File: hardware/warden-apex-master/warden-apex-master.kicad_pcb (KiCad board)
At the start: 4 copper layers, 100 x 100 mm, 88 parts, among them IC1 SIM7080G, IC2 BQ24650RVAR, IC3 TPS63070RNMR, IC4 MAX98357AETE+T, J1 U.FL-R-SMT-1, J2 U.FL-R-SMT-1, J3 61300211121, J4 Expansion_Header, J5 Qwiic, Q1 DMG9926UDM, Q2 AO3401A, Q3 2N7002, U1 113991115, U2 Ai-Thinker-Ra-01, U3 M138 Modem, U4 MCP23017_SO, U5 SRV05-4-P-T7, U6 SC16IS740, X1 14.7456MHz

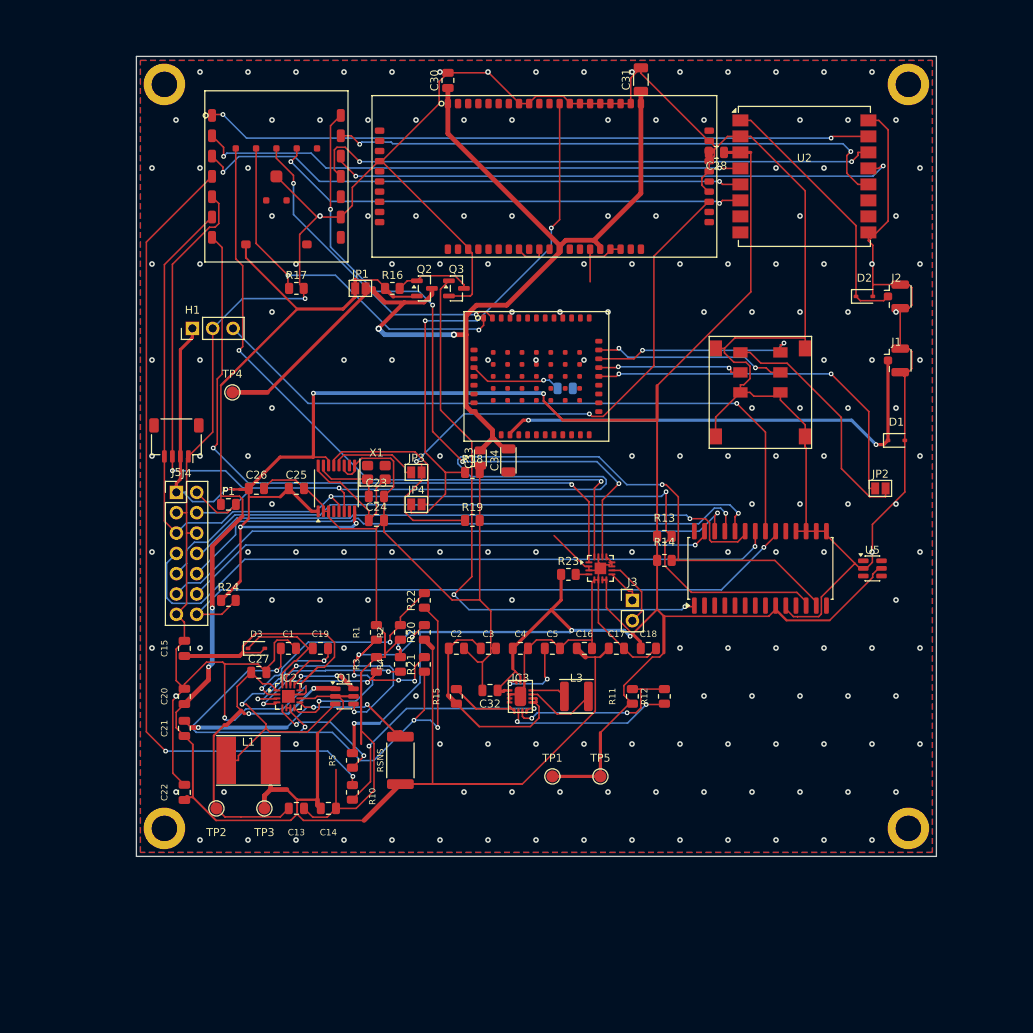
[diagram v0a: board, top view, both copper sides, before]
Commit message: Update warden-apex design to Phase 24 live state. Enhanced README.md to clarify current design status, noting that the snapshot is not yet production-ready. Adjusted BOM files to include additional resistors and capacitors, and updated component placements. Revised Gerber files with new timestamps and ensured consistency across documentation. Addressed DRC issues with 10 violations and 5 unconnected items, indicating further cleanup is required before production submission.
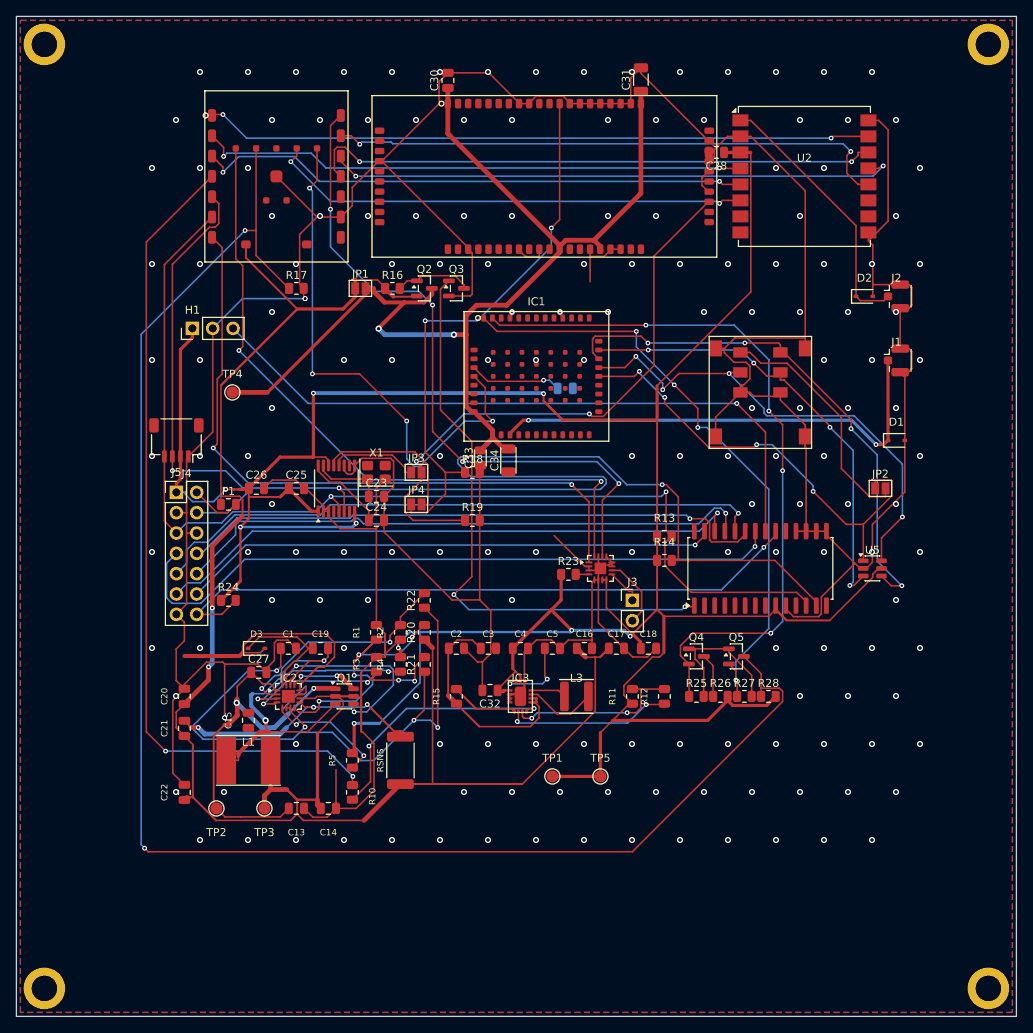
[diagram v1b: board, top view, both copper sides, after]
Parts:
- added Q4: SOT-23, SOT-23, F.Cu at (70.0, 75.0)
- added Q5: SOT-23, SOT-23, F.Cu at (75.0, 75.0)
- added R25: R_0805_2012Metric, R_0805_2012Metric, F.Cu at (70.0, 80.0)
- added R26: R_0805_2012Metric, R_0805_2012Metric, F.Cu at (73.0, 80.0)
- added R27: R_0805_2012Metric, R_0805_2012Metric, F.Cu at (76.0, 80.0)
- added R28: R_0805_2012Metric, R_0805_2012Metric, F.Cu at (79.0, 80.0)
- C31, C34: value 47uF -> 220uF
- IC1: value SIM7080G -> LCC-42_SIM7080G; footprint warden_custom:LCC-42_SIM7080G -> LCC-42_SIM7080G
- moved MH3 25.0 mm to (-11.5, 116.5)
- moved MH4 22.4 mm to (106.5, 116.5)
- moved MH1 15.8 mm to (-11.5, -1.50)
- moved C15 12.0 mm to (14.0, 83.0)
- moved MH2 11.2 mm to (106.5, -1.50)
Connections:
- IC1 pad 1: /UART1_RX -> /UART1_RX_1V8
- IC1 pad 2: /UART1_TX -> /UART1_TX_1V8
- J5 pad MP: (no net) -> /DUMMY_NET_PRESERVE_2
- MH1 pad : (no net) -> /DUMMY_NET_PRESERVE_0
- MH2 pad : (no net) -> /DUMMY_NET_PRESERVE_113
- MH3 pad : (no net) -> /DUMMY_NET_PRESERVE_114
- MH4 pad : (no net) -> /DUMMY_NET_PRESERVE_3
- U1 pad 12: (no net) -> /DUMMY_NET_PRESERVE_8
- U1 pad 14: (no net) -> /DUMMY_NET_PRESERVE_9
- U1 pad 16: (no net) -> /DUMMY_NET_PRESERVE_10
- U1 pad 21: (no net) -> /MODEM_PWRKEY_N
- U1 pad 22: (no net) -> /DUMMY_NET_PRESERVE_11
- U1 pad 23: (no net) -> /DUMMY_NET_PRESERVE_12
- U2 pad 10: (no net) -> /DUMMY_NET_PRESERVE_52
- U2 pad 11: (no net) -> /DUMMY_NET_PRESERVE_53
- U2 pad 7: (no net) -> /DUMMY_NET_PRESERVE_50
- U2 pad 8: (no net) -> /DUMMY_NET_PRESERVE_51
- U3 pad 10: (no net) -> /DUMMY_NET_PRESERVE_19
- U3 pad 11: (no net) -> /DUMMY_NET_PRESERVE_20
- U3 pad 2: (no net) -> /DUMMY_NET_PRESERVE_13
- U3 pad 21: (no net) -> /DUMMY_NET_PRESERVE_21
- U3 pad 26: (no net) -> /DUMMY_NET_PRESERVE_22
- U3 pad 29: (no net) -> /DUMMY_NET_PRESERVE_23
- U3 pad 3: (no net) -> /DUMMY_NET_PRESERVE_14
- U3 pad 30: (no net) -> /DUMMY_NET_PRESERVE_24
- U3 pad 31: (no net) -> /DUMMY_NET_PRESERVE_25
- U3 pad 32: (no net) -> /DUMMY_NET_PRESERVE_26
- U3 pad 37: (no net) -> /DUMMY_NET_PRESERVE_27
- U3 pad 38: (no net) -> /DUMMY_NET_PRESERVE_28
- U3 pad 4: (no net) -> /DUMMY_NET_PRESERVE_15
- U3 pad 40: (no net) -> /DUMMY_NET_PRESERVE_29
- U3 pad 42: (no net) -> /DUMMY_NET_PRESERVE_30
- U3 pad 44: (no net) -> /DUMMY_NET_PRESERVE_31
- U3 pad 45: (no net) -> /DUMMY_NET_PRESERVE_32
- U3 pad 46: (no net) -> /DUMMY_NET_PRESERVE_33
- U3 pad 47: (no net) -> /DUMMY_NET_PRESERVE_34
- U3 pad 49: (no net) -> /DUMMY_NET_PRESERVE_35
- U3 pad 5: (no net) -> /DUMMY_NET_PRESERVE_16
- U3 pad 50: (no net) -> /DUMMY_NET_PRESERVE_36
- U3 pad 51: (no net) -> /DUMMY_NET_PRESERVE_37
- U3 pad 52: (no net) -> /DUMMY_NET_PRESERVE_38
- U3 pad 53: (no net) -> /DUMMY_NET_PRESERVE_39
- U3 pad 54: (no net) -> /DUMMY_NET_PRESERVE_40
- U3 pad 55: (no net) -> /DUMMY_NET_PRESERVE_41
- U3 pad 56: (no net) -> /DUMMY_NET_PRESERVE_42
- U3 pad 58: (no net) -> /DUMMY_NET_PRESERVE_43
- U3 pad 59: (no net) -> /DUMMY_NET_PRESERVE_44
- U3 pad 6: (no net) -> /DUMMY_NET_PRESERVE_17
- U3 pad 60: (no net) -> /DUMMY_NET_PRESERVE_45
- U3 pad 7: (no net) -> /DUMMY_NET_PRESERVE_18
- U4 pad 11: (no net) -> /DUMMY_NET_PRESERVE_61
- U4 pad 14: (no net) -> /DUMMY_NET_PRESERVE_62
- U4 pad 19: (no net) -> /DUMMY_NET_PRESERVE_63
- U4 pad 2: (no net) -> /DUMMY_NET_PRESERVE_54
- U4 pad 28: (no net) -> /DUMMY_NET_PRESERVE_64
- U4 pad 3: (no net) -> /DUMMY_NET_PRESERVE_55
- U4 pad 4: (no net) -> /DUMMY_NET_PRESERVE_56
- U4 pad 5: (no net) -> /DUMMY_NET_PRESERVE_57
- U4 pad 6: (no net) -> /DUMMY_NET_PRESERVE_58
- U4 pad 7: (no net) -> /DUMMY_NET_PRESERVE_59
- U4 pad 8: (no net) -> /DUMMY_NET_PRESERVE_60
- U5 pad 1: (no net) -> /SIM_VDD
- U5 pad 3: (no net) -> /SIM_DATA
- U5 pad 4: (no net) -> /SIM_CLK
- U5 pad 6: (no net) -> /SIM_RST
- U6 pad 10: (no net) -> /DUMMY_NET_PRESERVE_67
- U6 pad 4: (no net) -> /DUMMY_NET_PRESERVE_65
- U6 pad 7: (no net) -> /DUMMY_NET_PRESERVE_66
- X1 pad 3: (no net) -> /DUMMY_NET_PRESERVE_111
- X1 pad 4: (no net) -> /DUMMY_NET_PRESERVE_112
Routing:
- net /UART1_RX: track 47.7 -> 201.1 mm
- net /UART1_TX_1V8: track 0.00 -> 91.0 mm, vias 0 -> 4
- net /UART1_RX_1V8: track 0.00 -> 77.1 mm, vias 0 -> 4
- net /MODEM_PWRKEY_N: track 0.00 -> 67.7 mm, vias 0 -> 4
- net /SIM_RST: track 18.2 -> 61.2 mm, vias 2 -> 4
- net /SIM_CLK: track 25.5 -> 66.8 mm, vias 2 -> 4
- net /UART1_TX: track 39.7 -> 5.48 mm, vias 2 -> 0
- net /SIM_DATA: track 24.0 -> 57.1 mm, vias 2 -> 4
- net /3V3: track 404.5 -> 427.1 mm
- net /VDD_EXT: track 0.00 -> 18.5 mm
- net /SIM_VDD: track 46.2 -> 57.2 mm, vias 2 -> 4
- net /GND: track 646.2 -> 636.4 mm, vias 173 -> 334
- net /SOLAR_IN: track 47.0 -> 49.6 mm
- net /REG_EN: track 13.1 -> 12.3 mm
- net /CHG_PH: track 42.1 -> 41.3 mm
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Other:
- board size 100 x 100 mm -> 125 x 125 mm

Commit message: Remove obsolete ERC report file and update README.md to reflect the current post-repair release snapshot. Adjusted DRC results to indicate zero violations and unconnected items, confirming readiness for fabrication. Updated Gerber files with new timestamps for consistency across documentation.
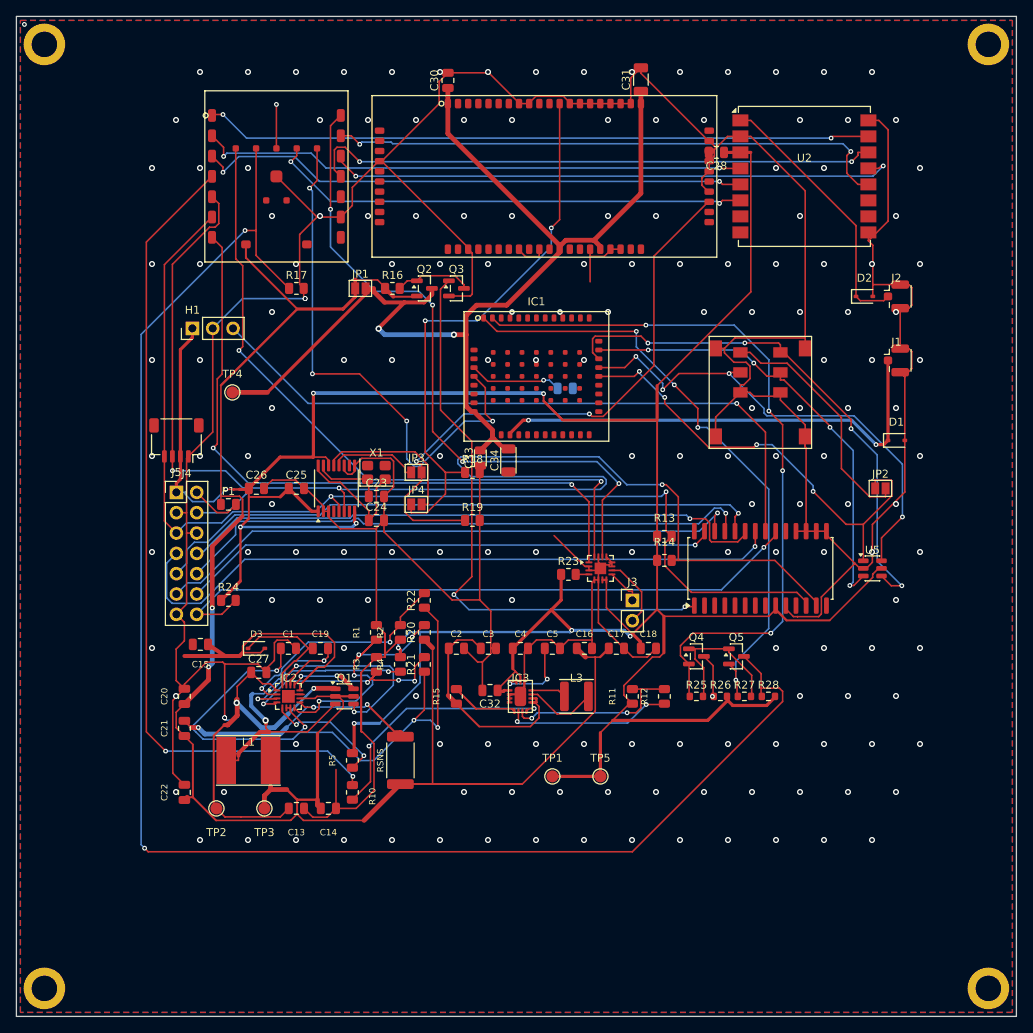
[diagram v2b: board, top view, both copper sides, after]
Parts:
- R25, R26, R27, R28: footprint R_0805_2012Metric -> R_0603_1608Metric
- moved C15 11.2 mm to (8.00, 73.5), turned to 180 degrees
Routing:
- net /UART1_TX: track 5.48 -> 234.6 mm, vias 0 -> 2
- net /GND: track 636.4 -> 631.2 mm, vias 334 -> 331
- net /CHG_REGN: track 32.6 -> 35.2 mm

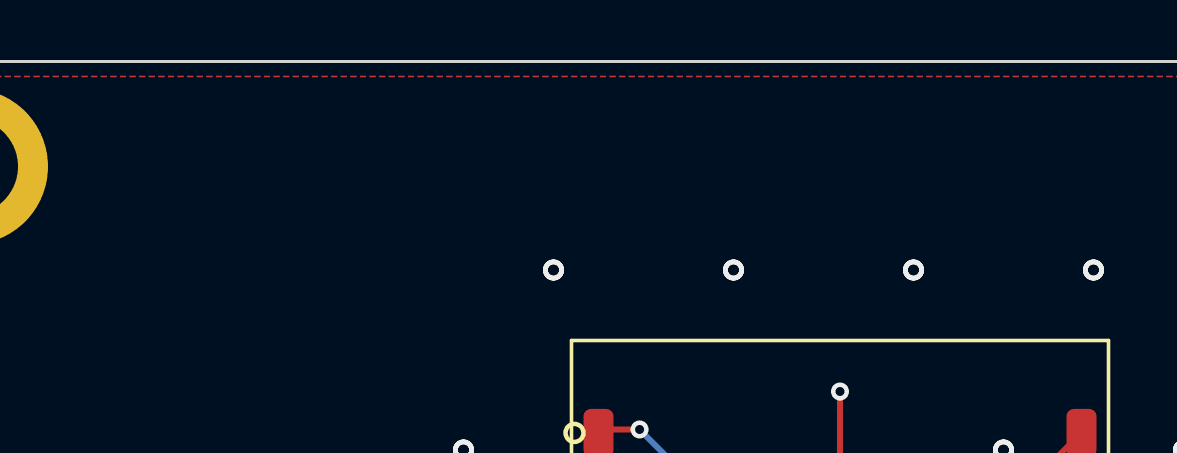
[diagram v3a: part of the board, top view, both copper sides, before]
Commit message: Update warden-apex design with new components and adjustments to BOM files. Added capacitors C35 and C36, and resistor R30, while updating references for existing components. Revised Gerber files with new timestamps for consistency and ensured all documentation reflects the latest design changes.
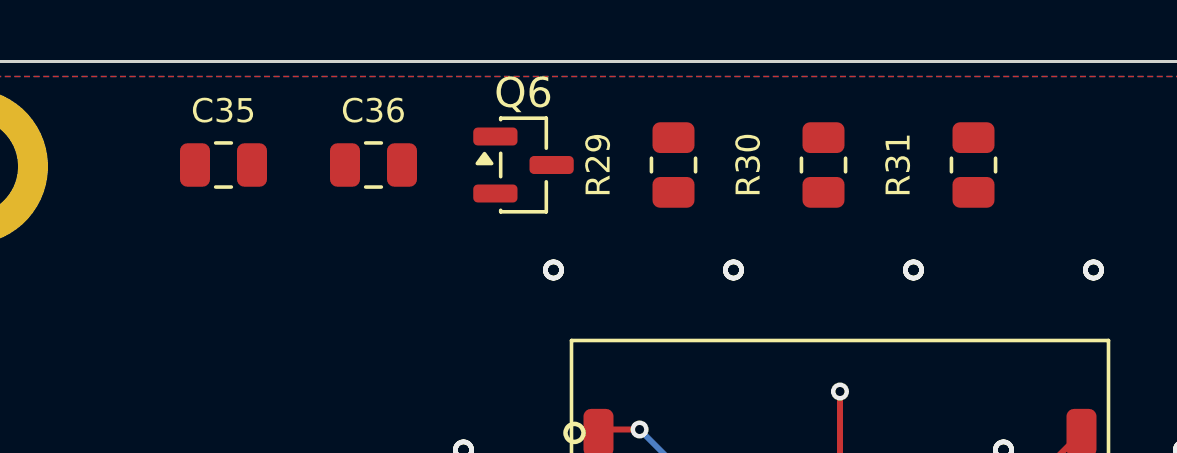
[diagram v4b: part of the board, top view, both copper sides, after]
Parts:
- added C35: 100nF, Capacitor_SMD:C_0805_2012Metric, F.Cu at (-3.05, -1.55)
- added C36: 100nF, Capacitor_SMD:C_0805_2012Metric, F.Cu at (1.95, -1.55)
- added Q6: 2N7002, Package_TO_SOT_SMD:SOT-23, F.Cu at (6.95, -1.55)
- added R29: 10kΩ, Resistor_SMD:R_0805_2012Metric, F.Cu at (11.9, -1.55)
- added R30: 10kΩ, Resistor_SMD:R_0805_2012Metric, F.Cu at (16.9, -1.55)
- added R31: 10kΩ, Resistor_SMD:R_0805_2012Metric, F.Cu at (21.9, -1.55)

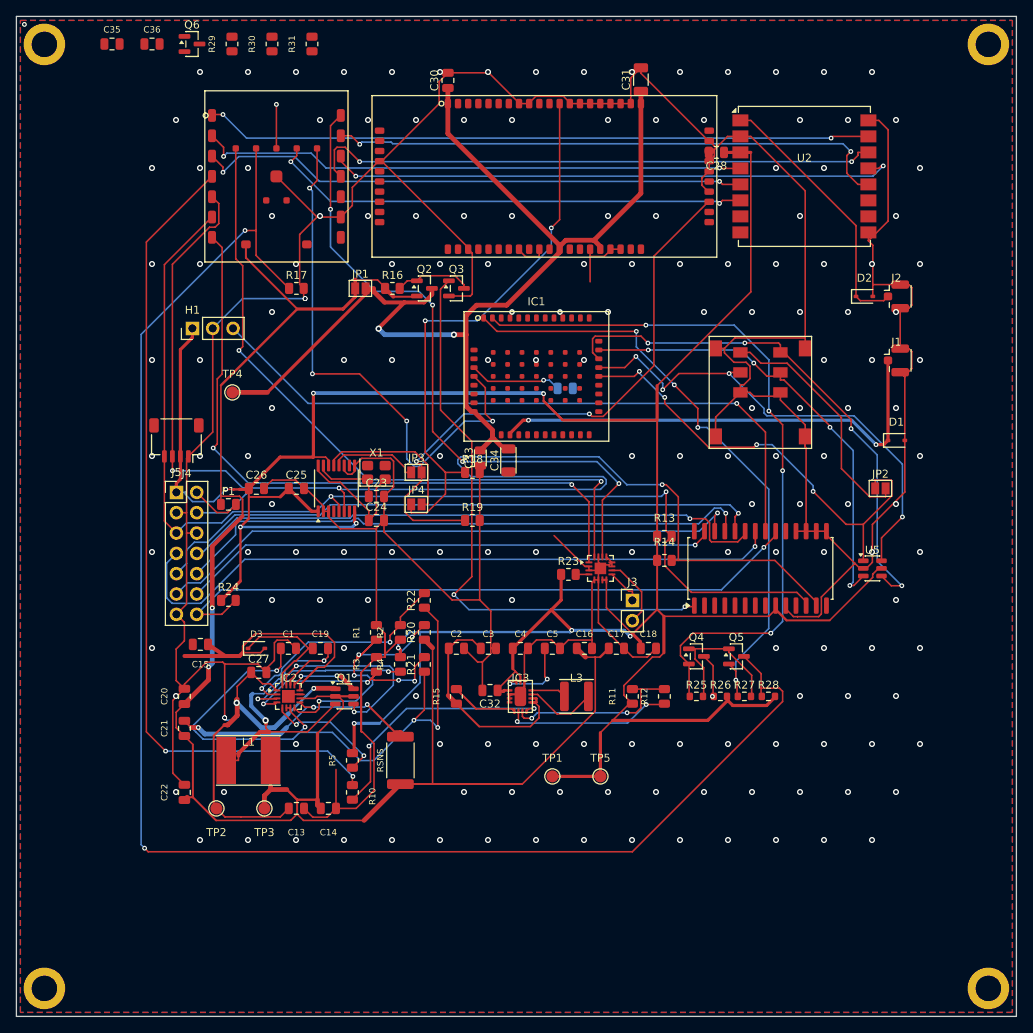
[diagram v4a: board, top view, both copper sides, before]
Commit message: Update warden-apex design with revised DRC and ERC results, reflecting current warnings and violations. Adjusted README.md to clarify design status and known caveats. Updated Gerber files with new timestamps for consistency. Renamed components in the master position file for clarity and improved organization.
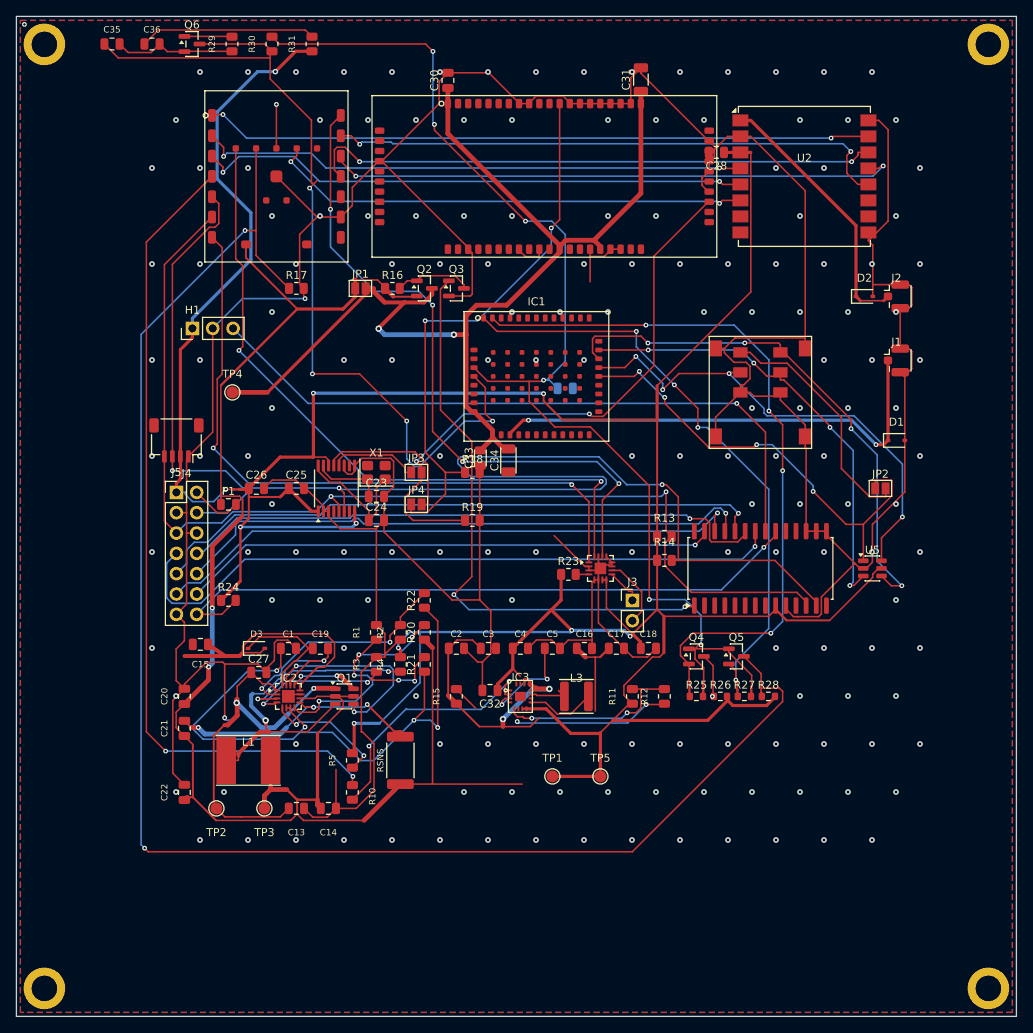
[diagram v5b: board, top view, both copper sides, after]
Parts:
- IC3: footprint warden_custom:QFN-15-1EP_3x4mm_P0.5mm_EP1.45x2.45mm -> TPS63070_RNM0015A
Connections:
- IC3 pad 1: /3V3 -> /GND
- IC3 pad 10: /FB2_LINK -> /GND
- IC3 pad 11: /FB_DIV -> /SW_A
- IC3 pad 12: /PGOOD -> /REG_IN
- IC3 pad 13: /VAUX -> /REG_IN
- IC3 pad 14: /3V3 -> /REG_EN
- IC3 pad 2: /GND -> /PGOOD
- IC3 pad 3: /GND -> /VAUX
- IC3 pad 5: /SW_A -> /FB_DIV
- IC3 pad 6: /SW_B -> /FB2_LINK
- IC3 pad 7: /REG_IN -> /3V3
- IC3 pad 8: /REG_IN -> /3V3
- IC3 pad 9: /REG_EN -> /SW_B
- Q4 pad 1: /VDD_EXT -> /SIM_VDD_EXT
- Q5 pad 1: /VDD_EXT -> /SIM_VDD_EXT
- R25 pad 2: /VDD_EXT -> /SIM_VDD_EXT
- R27 pad 2: /VDD_EXT -> /SIM_VDD_EXT
- U1 pad 21: /MODEM_PWRKEY_N -> /XIAO_EN
- U4 pad 18: /GND -> /EXP_RESET_N
- U4 pad 2: /DUMMY_NET_PRESERVE_54 -> /MODEM_PWRKEY_DRV
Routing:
- net /SIM_VDD_EXT: track 11.6 -> 153.1 mm, vias 1 -> 6
- net /MODEM_PWRKEY_N: track 67.7 -> 113.5 mm
- net /VBAT_SYS: track 249.4 -> 215.9 mm
- net /GND: track 631.2 -> 607.6 mm, vias 331 -> 166
- net /EXP_RESET_N: track 0.00 -> 22.0 mm
- net /VDD_EXT: track 18.5 -> 0.00 mm
- net GND: track 0.00 -> 15.3 mm
- net /3V3: track 427.1 -> 439.6 mm, vias 9 -> 10
- net /REG_IN: track 28.6 -> 37.8 mm, vias 0 -> 2
- net /REG_EN: track 12.3 -> 3.48 mm
- net /MODEM_PWRKEY_DRV: track 0.00 -> 5.95 mm
- net /CHG_VFB: track 35.2 -> 31.3 mm
- net /VAUX: track 9.78 -> 12.5 mm
- net /UART1_TX_1V8: track 91.0 -> 93.0 mm
- net /TS_BIAS: track 28.4 -> 26.9 mm
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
